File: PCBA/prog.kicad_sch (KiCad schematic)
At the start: 4 parts

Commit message: More schematics
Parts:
- J601: renamed from J?; footprint (none) -> Connector_USB:USB_C_Receptacle_HRO_TYPE-C-31-M-12
- R601, R602: renamed from R?; footprint (none) -> Resistor_SMD:R_0603_1608Metric
- gave numbers to parts that had none: 1
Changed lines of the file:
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@@
   (symbol (lib_id "power:GND") (at 73.66 78.74 0) (unit 1)
     (in_bom yes) (on_board yes) (fields_autoplaced)
-    (property "Reference" "#PWR?" (id 0) (at 73.66 85.09 0)
+    (property "Reference" "#PWR0136" (id 0) (at 73.66 85.09 0)
       (effects (font (size 1.27 1.27)) hide)
     )
@@
   (symbol (lib_id "power:GND") (at 114.3 48.26 0) (unit 1)
     (in_bom yes) (on_board yes) (fields_autoplaced)
-    (property "Reference" "#PWR?" (id 0) (at 114.3 54.61 0)
+    (property "Reference" "#PWR0138" (id 0) (at 114.3 54.61 0)
       (effects (font (size 1.27 1.27)) hide)
     )
@@
   (symbol (lib_id "Device:R") (at 105.41 48.26 270) (unit 1)
     (in_bom yes) (on_board yes)
-    (property "Reference" "R?" (id 0) (at 105.41 50.8 90))
+    (property "Reference" "R602" (id 0) (at 105.41 50.8 90))
     (property "Value" "5.1k" (id 1) (at 105.41 48.26 90))
-    (property "Footprint" "" (id 2) (at 105.41 46.482 90)
+    (property "Footprint" "Resistor_SMD:R_0603_1608Metric" (id 2) (at 105.41 46.482 90)
       (effects (font (size 1.27 1.27)) hide)
     )
@@
   (symbol (lib_id "power:VDD") (at 161.29 41.91 0) (unit 1)
     (in_bom yes) (on_board yes) (fields_autoplaced)
-    (property "Reference" "#PWR?" (id 0) (at 161.29 45.72 0)
+    (property "Reference" "#PWR0135" (id 0) (at 161.29 45.72 0)
       (effects (font (size 1.27 1.27)) hide)
     )
@@
   (symbol (lib_id "power:GND") (at 163.83 72.39 0) (unit 1)
     (in_bom yes) (on_board yes) (fields_autoplaced)
-    (property "Reference" "#PWR?" (id 0) (at 163.83 78.74 0)
+    (property "Reference" "#PWR0133" (id 0) (at 163.83 78.74 0)
       (effects (font (size 1.27 1.27)) hide)
     )
@@
   (symbol (lib_id "power:VDD") (at 163.83 41.91 0) (unit 1)
     (in_bom yes) (on_board yes) (fields_autoplaced)
-    (property "Reference" "#PWR?" (id 0) (at 163.83 45.72 0)
+    (property "Reference" "#PWR0134" (id 0) (at 163.83 45.72 0)
       (effects (font (size 1.27 1.27)) hide)
     )
@@
   (symbol (lib_id "Interface_USB:CH340E") (at 163.83 57.15 0) (unit 1)
     (in_bom yes) (on_board yes) (fields_autoplaced)
-    (property "Reference" "U?" (id 0) (at 165.8494 72.39 0)
+    (property "Reference" "U601" (id 0) (at 165.8494 72.39 0)
       (effects (font (size 1.27 1.27)) (justify left))
     )
@@
   (symbol (lib_id "Device:R") (at 105.41 45.72 90) (unit 1)
     (in_bom yes) (on_board yes)
-    (property "Reference" "R?" (id 0) (at 105.41 43.18 90))
+    (property "Reference" "R601" (id 0) (at 105.41 43.18 90))
     (property "Value" "5.1k" (id 1) (at 105.41 45.72 90))
-    (property "Footprint" "" (id 2) (at 105.41 47.498 90)
+    (property "Footprint" "Resistor_SMD:R_0603_1608Metric" (id 2) (at 105.41 47.498 90)
       (effects (font (size 1.27 1.27)) hide)
     )
@@
   (symbol (lib_id "power:GND") (at 66.04 78.74 0) (unit 1)
     (in_bom yes) (on_board yes) (fields_autoplaced)
-    (property "Reference" "#PWR?" (id 0) (at 66.04 85.09 0)
+    (property "Reference" "#PWR0137" (id 0) (at 66.04 85.09 0)
       (effects (font (size 1.27 1.27)) hide)
     )
@@
   (symbol (lib_id "Connector:USB_C_Receptacle_USB2.0") (at 73.66 55.88 0) (unit 1)
     (in_bom yes) (on_board yes) (fields_autoplaced)
-    (property "Reference" "J?" (id 0) (at 73.66 35.56 0))
+    (property "Reference" "J601" (id 0) (at 73.66 35.56 0))
     (property "Value" "USB_C_Receptacle_USB2.0" (id 1) (at 74.9299 36.83 90)
       (effects (font (size 1.27 1.27)) (justify left) hide)
     )
-    (property "Footprint" "" (id 2) (at 77.47 55.88 0)
+    (property "Footprint" "Connector_USB:USB_C_Receptacle_HRO_TYPE-C-31-M-12" (id 2) (at 77.47 55.88 0)
       (effects (font (size 1.27 1.27)) hide)
     )

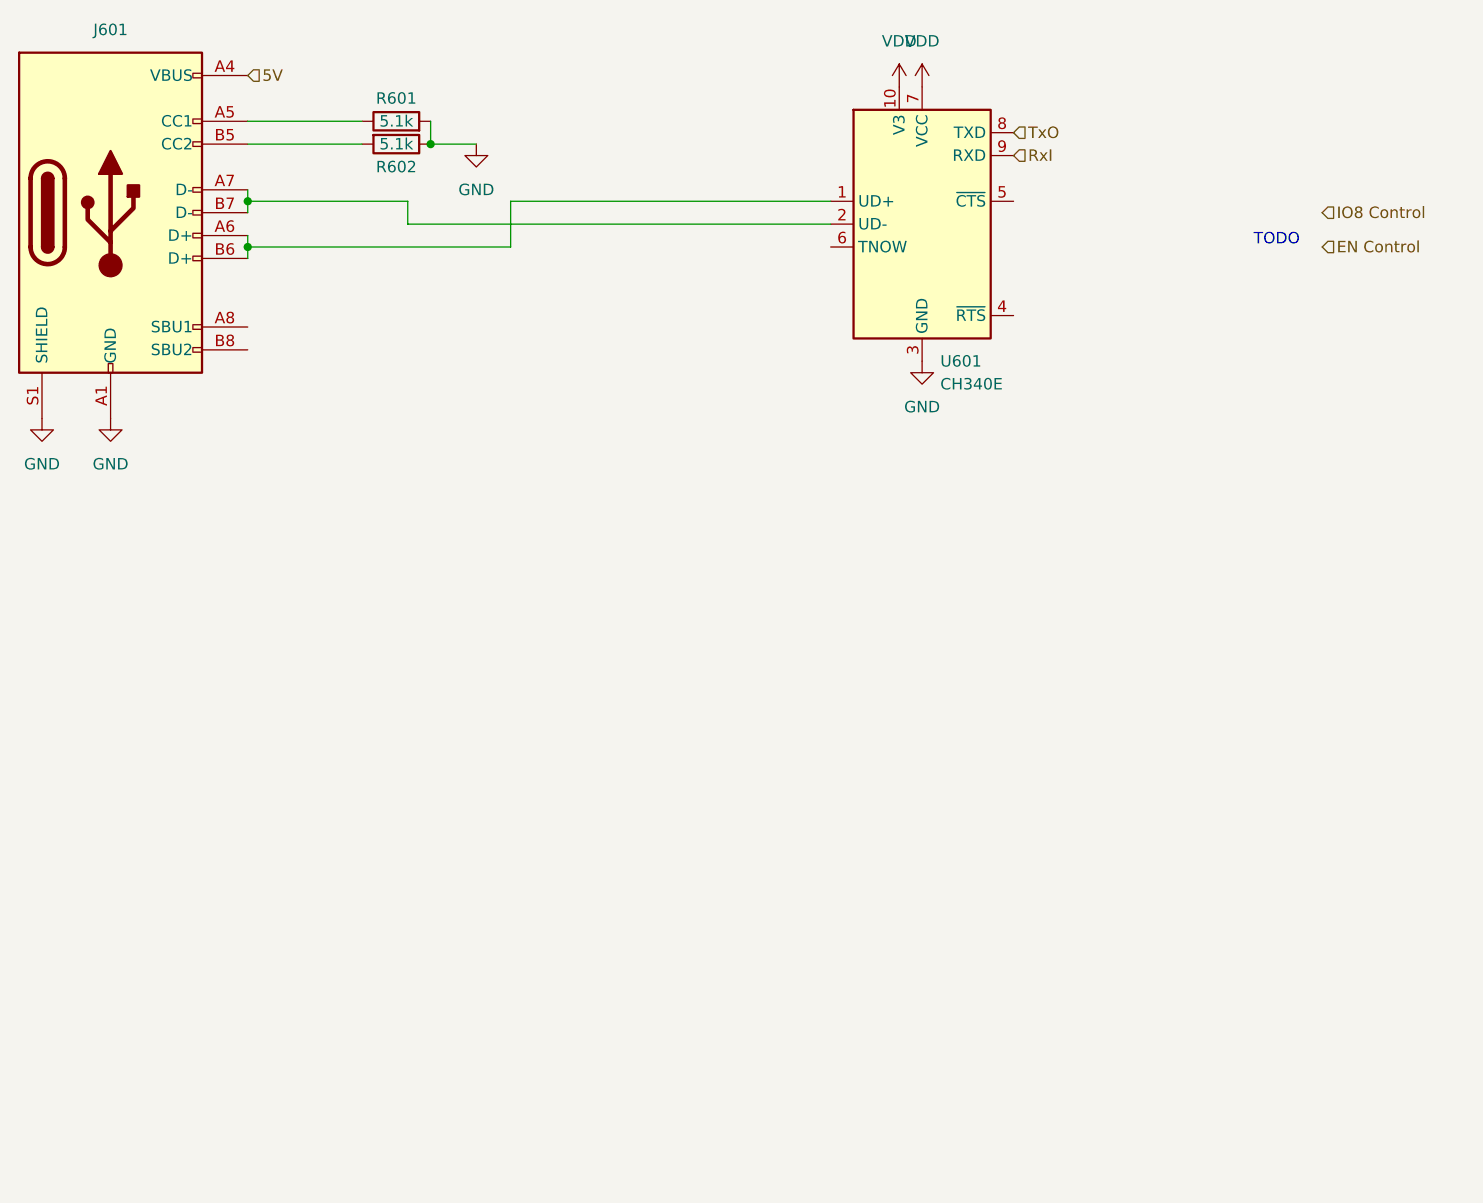
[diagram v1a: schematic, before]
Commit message: Update schematic pinmap bl706
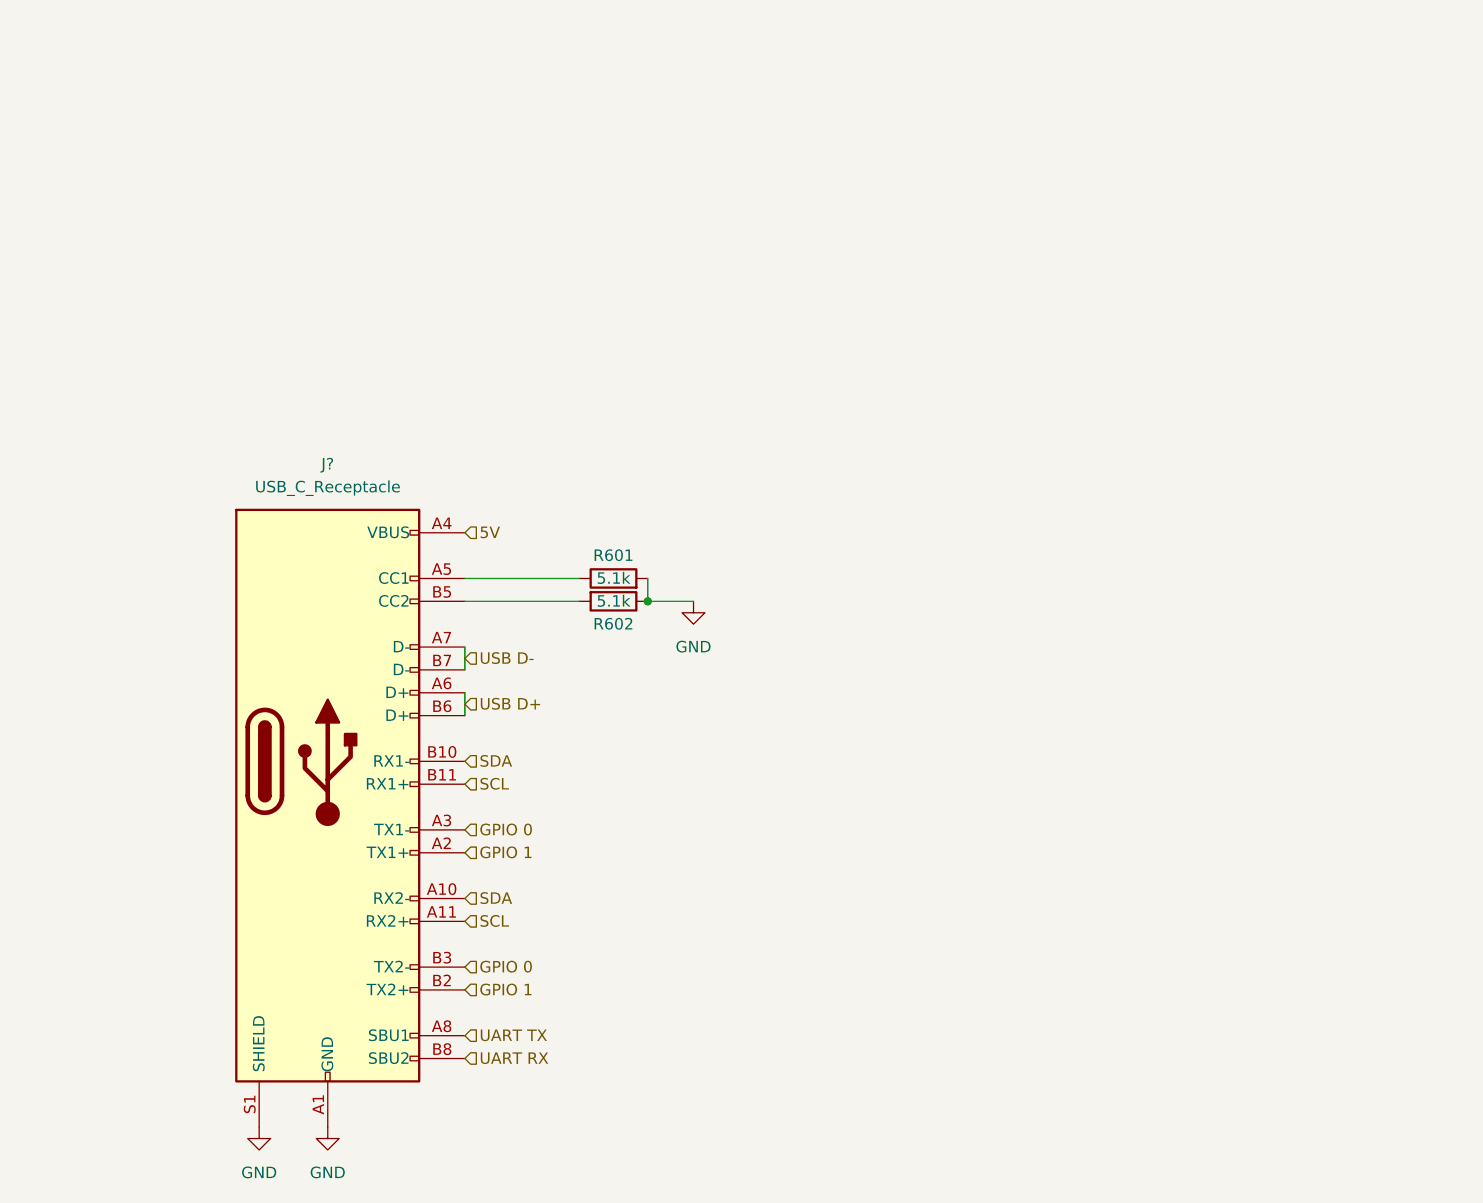
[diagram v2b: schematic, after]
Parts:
- removed J601: USB_C_Receptacle_USB2.0, Connector_USB:USB_C_Receptacle_HRO_TYPE-C-31-M-12, symbol Connector:USB_C_Receptacle_USB2.0
- removed U601: CH340E, Package_SO:MSOP-10_3x3mm_P0.5mm, symbol Interface_USB:CH340E
- added J?: USB_C_Receptacle, Connector_USB:USB_C_Receptacle_Amphenol_12401610E4-2A, symbol Connector:USB_C_Receptacle
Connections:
- net 5V: now also J?.A4 (VBUS), J?.A9 (VBUS), J?.B4 (VBUS), J?.B9 (VBUS)
- net GND: now also J?.A1 (GND), J?.A12 (GND), J?.B1 (GND), J?.B12 (GND), J?.S1 (SHIELD)
- net at R602.2: now also J?.B5 (CC2)
- net at R601.1: now also J?.A5 (CC1)
- new net GPIO 0: J?.A3 (TX1-), J?.B3 (TX2-)
- new net GPIO 1: J?.A2 (TX1+), J?.B2 (TX2+)
- new net SCL: J?.A11 (RX2+), J?.B11 (RX1+)
- new net SDA: J?.A10 (RX2-), J?.B10 (RX1-)
- new net UART RX: J?.B8 (SBU2)
- new net UART TX: J?.A8 (SBU1)
- new net USB D+: J?.A6 (D+), J?.B6 (D+)
- new net USB D-: J?.A7 (D-), J?.B7 (D-)
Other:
- note removed: "TODO"
- moved on the sheet: R601, R602

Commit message: .
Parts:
- gave numbers to parts that had none: 1
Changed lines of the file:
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@@
   (symbol (lib_id "Connector:USB_C_Receptacle") (at 97.79 116.84 0) (unit 1)
     (in_bom yes) (on_board yes) (fields_autoplaced)
-    (property "Reference" "J?" (id 0) (at 97.79 83.82 0))
+    (property "Reference" "J601" (id 0) (at 97.79 83.82 0))
     (property "Value" "USB_C_Receptacle" (id 1) (at 97.79 86.36 0))
     (property "Footprint" "Connector_USB:USB_C_Receptacle_Amphenol_12401610E4-2A" (id 2) (at 101.6 116.84 0)

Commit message: Routing
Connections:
- net GPIO 0: now also J601.A10 (RX2-); no longer J601.A3 (TX1-)
- net GPIO 1: now also J601.A11 (RX2+); no longer J601.A2 (TX1+)
- net SCL: now also J601.A2 (TX1+); no longer J601.A11 (RX2+)
- net SDA: now also J601.A3 (TX1-); no longer J601.A10 (RX2-)
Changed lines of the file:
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@@
     (stroke (width 0) (type default) (color 0 0 0 0))
   )
-  (hierarchical_label "SDA" (shape input) (at 113.03 132.08 0)
+  (hierarchical_label "SDA" (shape input) (at 113.03 124.46 0)
     (effects (font (size 1.27 1.27)) (justify left))
   )
-  (hierarchical_label "GPIO 1" (shape input) (at 113.03 127 0)
+  (hierarchical_label "GPIO 1" (shape input) (at 113.03 134.62 0)
     (effects (font (size 1.27 1.27)) (justify left))
   )
-  (hierarchical_label "GPIO 0" (shape input) (at 113.03 124.46 0)
+  (hierarchical_label "GPIO 0" (shape input) (at 113.03 132.08 0)
     (effects (font (size 1.27 1.27)) (justify left))
   )
@@
     (effects (font (size 1.27 1.27)) (justify left))
   )
-  (hierarchical_label "SCL" (shape input) (at 113.03 134.62 0)
+  (hierarchical_label "SCL" (shape input) (at 113.03 127 0)
     (effects (font (size 1.27 1.27)) (justify left))
   )

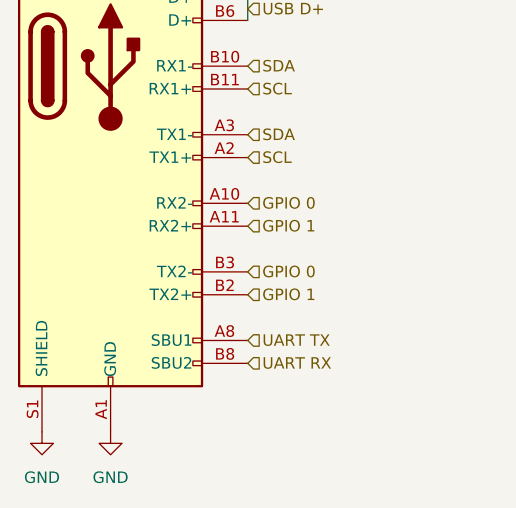
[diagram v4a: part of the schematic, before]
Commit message: Jtag on usb-c
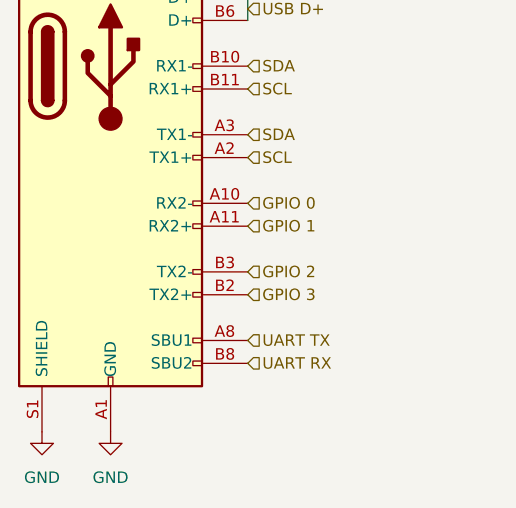
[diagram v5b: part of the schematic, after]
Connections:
- net GPIO 0: no longer J601.B3 (TX2-)
- net GPIO 1: no longer J601.B2 (TX2+)
- new net GPIO 2: J601.B3 (TX2-)
- new net GPIO 3: J601.B2 (TX2+)
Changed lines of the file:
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@@
     (effects (font (size 1.27 1.27)) (justify left))
   )
-  (hierarchical_label "GPIO 1" (shape input) (at 113.03 142.24 0)
+  (hierarchical_label "GPIO 3" (shape input) (at 113.03 142.24 0)
     (effects (font (size 1.27 1.27)) (justify left))
   )
@@
     (effects (font (size 1.27 1.27)) (justify left))
   )
-  (hierarchical_label "GPIO 0" (shape input) (at 113.03 139.7 0)
+  (hierarchical_label "GPIO 2" (shape input) (at 113.03 139.7 0)
     (effects (font (size 1.27 1.27)) (justify left))
   )
